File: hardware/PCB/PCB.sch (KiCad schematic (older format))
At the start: 0 parts

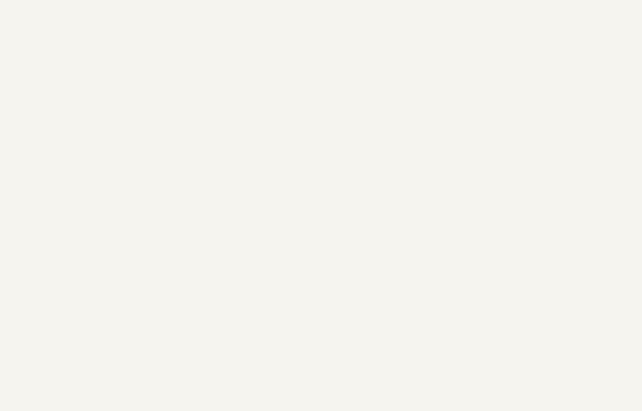
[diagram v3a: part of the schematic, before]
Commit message: 0.6 I hate these auto generated code from STM32Cube
1. ready for the firmware nightmare
2. adjust the M3 screw holes
3. add tooling holes for future PCBA
4. if nothing go wrong, this will be the V1 after testing
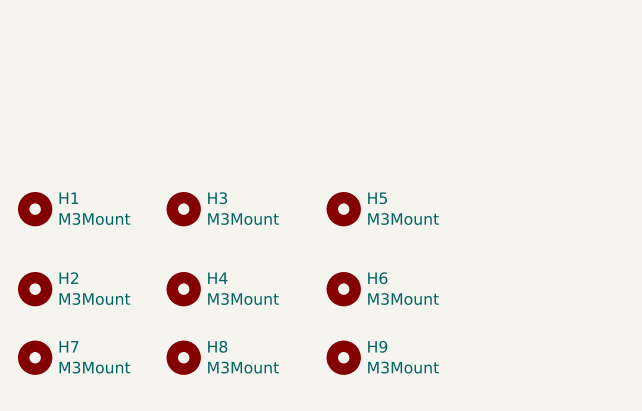
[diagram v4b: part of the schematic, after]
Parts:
- added H1, H2, H3, H4, H5, H6: M3Mount, MountingHole:MountingHole_3.2mm_M3_DIN965, symbol Mechanical:MountingHole
- added H7, H8, H9: M3Mount, KiCad:JLC_SMT_ToolingHole, symbol Mechanical:MountingHole
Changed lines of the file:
@@
 Sheet 1 6
 Title "NHW68"
-Date "2020-02-08"
-Rev "0.5"
+Date "2020-02-10"
+Rev "0.6"
 Comp ""
 Comment1 ""
@@
 Wire Wire Line
 	6250 4950 5200 4950
+$Comp
+L Mechanical:MountingHole H4
+U 1 1 5E422B05
+P 1600 4700
+F 0 "H4" H 1700 4746 50  0000 L CNN
+F 1 "M3Mount" H 1700 4655 50  0000 L CNN
+F 2 "MountingHole:MountingHole_3.2mm_M3_DIN965" H 1600 4700 50  0001 C CNN
+F 3 "~" H 1600 4700 50  0001 C CNN
+	1    1600 4700
+	1    0    0    -1
+$EndComp
+$Comp
+L Mechanical:MountingHole H2
+U 1 1 5E423012
+P 950 4700
+F 0 "H2" H 1050 4746 50  0000 L CNN
+F 1 "M3Mount" H 1050 4655 50  0000 L CNN
+F 2 "MountingHole:MountingHole_3.2mm_M3_DIN965" H 950 4700 50  0001 C CNN
+F 3 "~" H 950 4700 50  0001 C CNN
+	1    950  4700
+	1    0    0    -1
+$EndComp
+$Comp
+L Mechanical:MountingHole H1
+U 1 1 5E423452
+P 950 4350
+F 0 "H1" H 1050 4396 50  0000 L CNN
+F 1 "M3Mount" H 1050 4305 50  0000 L CNN
+F 2 "MountingHole:MountingHole_3.2mm_M3_DIN965" H 950 4350 50  0001 C CNN
+F 3 "~" H 950 4350 50  0001 C CNN
+	1    950  4350
+	1    0    0    -1
+$EndComp
+$Comp
+L Mechanical:MountingHole H3
+U 1 1 5E42389A
+P 1600 4350
+F 0 "H3" H 1700 4396 50  0000 L CNN
+F 1 "M3Mount" H 1700 4305 50  0000 L CNN
+F 2 "MountingHole:MountingHole_3.2mm_M3_DIN965" H 1600 4350 50  0001 C CNN
+F 3 "~" H 1600 4350 50  0001 C CNN
+	1    1600 4350
+	1    0    0    -1
+$EndComp
+$Comp
+L Mechanical:MountingHole H6
+U 1 1 5E4291C7
+P 2300 4700
+F 0 "H6" H 2400 4746 50  0000 L CNN
+F 1 "M3Mount" H 2400 4655 50  0000 L CNN
+F 2 "MountingHole:MountingHole_3.2mm_M3_DIN965" H 2300 4700 50  0001 C CNN
+F 3 "~" H 2300 4700 50  0001 C CNN
+	1    2300 4700
+	1    0    0    -1
+$EndComp
+$Comp
+L Mechanical:MountingHole H5
+U 1 1 5E4291CD
+P 2300 4350
+F 0 "H5" H 2400 4396 50  0000 L CNN
+F 1 "M3Mount" H 2400 4305 50  0000 L CNN
+F 2 "MountingHole:MountingHole_3.2mm_M3_DIN965" H 2300 4350 50  0001 C CNN
+F 3 "~" H 2300 4350 50  0001 C CNN
+	1    2300 4350
+	1    0    0    -1
+$EndComp
+$Comp
+L Mechanical:MountingHole H8
+U 1 1 5E43E49C
+P 1600 5000
+F 0 "H8" H 1700 5046 50  0000 L CNN
+F 1 "M3Mount" H 1700 4955 50  0000 L CNN
+F 2 "KiCad:JLC_SMT_ToolingHole" H 1600 5000 50  0001 C CNN
+F 3 "~" H 1600 5000 50  0001 C CNN
+	1    1600 5000
+	1    0    0    -1
+$EndComp
+$Comp
+L Mechanical:MountingHole H7
+U 1 1 5E43E4A6
+P 950 5000
+F 0 "H7" H 1050 5046 50  0000 L CNN
+F 1 "M3Mount" H 1050 4955 50  0000 L CNN
+F 2 "KiCad:JLC_SMT_ToolingHole" H 950 5000 50  0001 C CNN
+F 3 "~" H 950 5000 50  0001 C CNN
+	1    950  5000
+	1    0    0    -1
+$EndComp
+$Comp
+L Mechanical:MountingHole H9
+U 1 1 5E43E4B0
+P 2300 5000
+F 0 "H9" H 2400 5046 50  0000 L CNN
+F 1 "M3Mount" H 2400 4955 50  0000 L CNN
+F 2 "KiCad:JLC_SMT_ToolingHole" H 2300 5000 50  0001 C CNN
+F 3 "~" H 2300 5000 50  0001 C CNN
+	1    2300 5000
+	1    0    0    -1
+$EndComp
 $EndSCHEMATC

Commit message: Remove some unused
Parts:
- H7, H8, H9: value M3Mount -> tooling
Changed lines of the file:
@@
 P 1600 5000
 F 0 "H8" H 1700 5046 50  0000 L CNN
-F 1 "M3Mount" H 1700 4955 50  0000 L CNN
+F 1 "tooling" H 1700 4955 50  0000 L CNN
 F 2 "KiCad:JLC_SMT_ToolingHole" H 1600 5000 50  0001 C CNN
 F 3 "~" H 1600 5000 50  0001 C CNN
@@
 P 950 5000
 F 0 "H7" H 1050 5046 50  0000 L CNN
-F 1 "M3Mount" H 1050 4955 50  0000 L CNN
+F 1 "tooling" H 1050 4955 50  0000 L CNN
 F 2 "KiCad:JLC_SMT_ToolingHole" H 950 5000 50  0001 C CNN
 F 3 "~" H 950 5000 50  0001 C CNN
@@
 P 2300 5000
 F 0 "H9" H 2400 5046 50  0000 L CNN
-F 1 "M3Mount" H 2400 4955 50  0000 L CNN
+F 1 "tooling" H 2400 4955 50  0000 L CNN
 F 2 "KiCad:JLC_SMT_ToolingHole" H 2300 5000 50  0001 C CNN
 F 3 "~" H 2300 5000 50  0001 C CNN
